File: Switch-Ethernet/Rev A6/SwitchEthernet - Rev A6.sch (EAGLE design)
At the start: 118 parts, among them J1 22-05-7028-02, J2 NE8FAV, J3 NE8FAV, J4 DF17(4.0)-20DS-0.5V(57), J5 DF17(4.0)-20DP-0.5V(57), J6 RB1-125BAG1A, T1 H1102FNL, T2 H1102FNL, T3 EXMACHINA-LOGO-NAME, U1 TC1264-3.3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

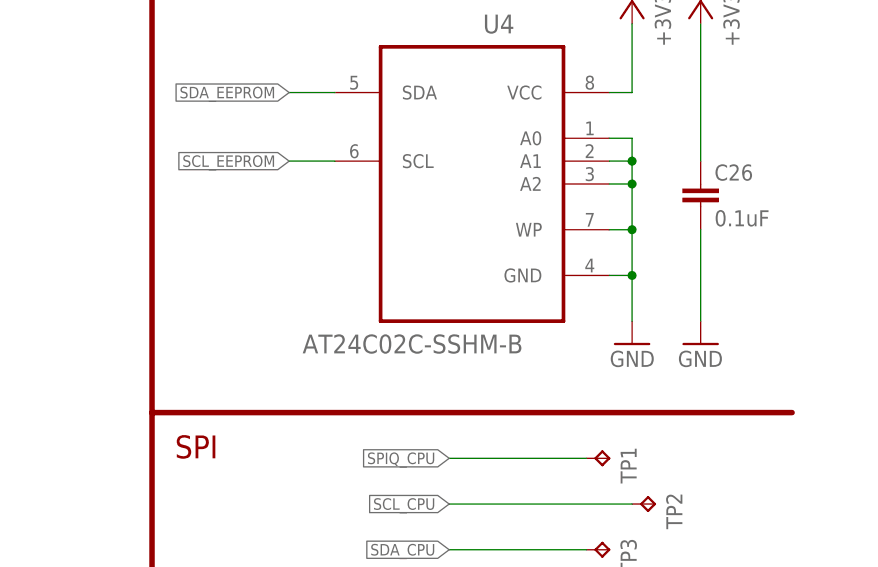
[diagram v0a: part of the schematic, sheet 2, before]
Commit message: generated MDP files of Ethernet switch rev A6
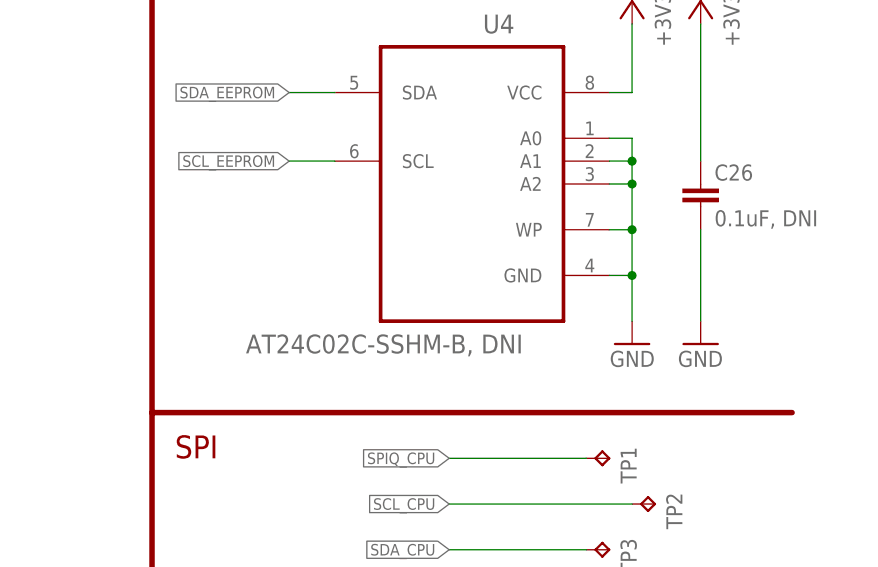
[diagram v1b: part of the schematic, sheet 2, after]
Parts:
- C1, C2, C5, C6: MF (none) -> MULTICOMP; OC_FARNELL unknown -> 1855909; OC_NEWARK 21T9879 -> unknown
- C10, C11, C12, C9: MF (none) -> MURATA; MPN MC0603B105K160CT -> GRM188R61C105KA93D; OC_FARNELL unknown -> 1828801; OC_NEWARK 06X6171 -> unknown
- C13, C14, C19: MF (none) -> KEMET; MPN MCCTA475M010 -> T491A475K016AT; OC_FARNELL unknown -> 1457428; OC_NEWARK 01M8221 -> unknown
- C15, C16, C17, C18, C20, C21, C25, C27, C28, C29, C30, C31, C32, C33, C34, C35, C36, C37, C38, C39, C4, C8: MF (none) -> MURATA; MPN MC0603B104K160CT -> GRM188R71H104KA93D; OC_FARNELL 1759037 -> 8820023; OC_NEWARK 06R4923 -> unknown
- C22, C24: MF (none) -> MURATA; MPN MC0603N180J500CT -> GRM1885C1H180JA01D; OC_FARNELL 1759006 -> 1828908; OC_NEWARK 06R5138 -> unknown
- C23, C3, C7: MF (none) -> MURATA; MPN GRM188R60J106ME47D -> GRM32DR71C106KA01L; OC_NEWARK 24R6334 -> unknown
- C26: value 0.1uF -> 0.1uF, DNI; MF (none) -> MURATA; MPN MC0603B104K160CT -> GRM188R71H104KA93D; OC_FARNELL 1759037 -> 8820023; OC_NEWARK 06R4923 -> unknown
- D1: MF (none) -> VISHAY; MPN (none) -> SMAJ33A-E3/61; OC_FARNELL 1812505 -> 9550909
- D2: MF (none) -> ON SEMICONDUCTOR; MPN 1N4148WS. -> 1N4148WS; OC_FARNELL unknown -> 2453269; OC_NEWARK 74M5710 -> unknown
- F1: MF (none) -> LITTELFUSE; MPN 1812L110/24DR -> 1206L050YR; OC_FARNELL (none) -> 1596993; OC_NEWARK 39X0319 -> unknown
- J1: MF (none) -> MOLEX; OC_NEWARK 25M1728 -> (none)
- J2, J3: OC_NEWARK 01M8373 -> unknown
- J4: MF (none) -> HIROSE(HRS); OC_FARNELL (none) -> 2300346; OC_NEWARK 69W0567 -> unknown
- J5: MF (none) -> HIROSE(HRS); OC_FARNELL (none) -> 2300344; OC_NEWARK 69W0566 -> unknown
- L1: MF (none) -> MURATA; OC_FARNELL unknown -> 1515461; OC_NEWARK 74M2809 -> unknown
- LED1: MF (none) -> MULTICOMP; OC_NEWARK 15R2206 -> unknown
- LED2, LED3, LED4, LED5: MF (none) -> MULTICOMP; OC_NEWARK 15R2205 -> unknown
- MP1, MP2, MP3, MP4, TP1, TP2, TP3, TP4, TP5: OC_FARNELL (none) -> unknown
- R1, R10, R11, R12, R13, R2, R4, R5, R6, R7, R8, R9: MF Multicomp Passives -> YAGEO; MPN MC0063W0603151R -> RC0603FR-0751RL; OC_FARNELL 2073520 -> 1799350; OC_NEWARK 58K4614 -> unknown
- R14, R15: MF Multicomp Passives -> YAGEO; MPN MC0063W0603175R -> RC0603FR-0775RL; OC_FARNELL 2073571 -> 1799355; OC_NEWARK 58K4654 -> unknown
- R16, R17, R18, R19: MF (none) -> YAGEO; MPN MCMR06X1001FTL -> RC0603FR-071KL.; OC_FARNELL 2073348 -> 2132444; OC_NEWARK 86T3505 -> unknown
- R20, R21, R22, R23, R24, R25, R26, R27, R30, R31, R32, R33: MF (none) -> MULTICOMP; MPN MC0603SAF499JT5E -> MCWR06X49R9FTL; OC_FARNELL 2073520 -> 2447381; OC_NEWARK 79M5983 -> unknown
- R28, R29: MF Multicomp Passives -> YAGEO (PHYCOMP); MPN MC0063W06031220R -> RC0603FR-07220RL; OC_FARNELL 2073428 -> 9238409; OC_NEWARK 58K4526 -> unknown
- R3: MF Multicomp Passives -> YAGEO; MPN MC0063W060311K5 -> RC0603FR-071K5L; OC_FARNELL 2073391 -> 2126808; OC_NEWARK 58K4488 -> unknown
- R34: MF Multicomp Passives -> YAGEO; MPN MC0063W0603110K -> RC0603FR-0710KL; OC_FARNELL 2073349 -> 2133286; OC_NEWARK 58K4450 -> unknown
- R35: MF (none) -> MULTICOMP; MPN MC0063W060313K01 -> MCMR06X3001FTL; OC_NEWARK 94W5780 -> unknown
- R36, R37: MF Multicomp Passives -> YAGEO; MPN MC0063W0603110K -> RC0603FR-0710KL; OC_FARNELL unknown -> 2133286; OC_NEWARK 58K4450 -> unknown
- R38, R39, R40, R41, R42, R43: MF Multicomp Passives -> YAGEO; MPN MC0603WG00000T5E-TC -> RC0603FR-070RL; OC_FARNELL unknown -> 2309106; OC_NEWARK 58K4684 -> unknown
- U1: MF MICROCHIP -> (none); MPN TC1264-3.3VDB -> (none)
- U2: MF MICROCHIP -> (none); MPN TC1264-1.8VDBTR -> (none); OC_NEWARK 92C5784 -> unknown
- U3: MF (none) -> MICROCHIP; MPN (none) -> KSZ8995MA
- U4: value AT24C02C-SSHM-B -> AT24C02C-SSHM-B, DNI; MF (none) -> MICROCHIP
- X1: MF (none) -> TXC; OC_NEWARK 84R5794 -> unknown
